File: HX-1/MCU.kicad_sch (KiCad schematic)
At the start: 27 parts, among them SW1 SW_SPDT, U1 STM32H723ZGT6

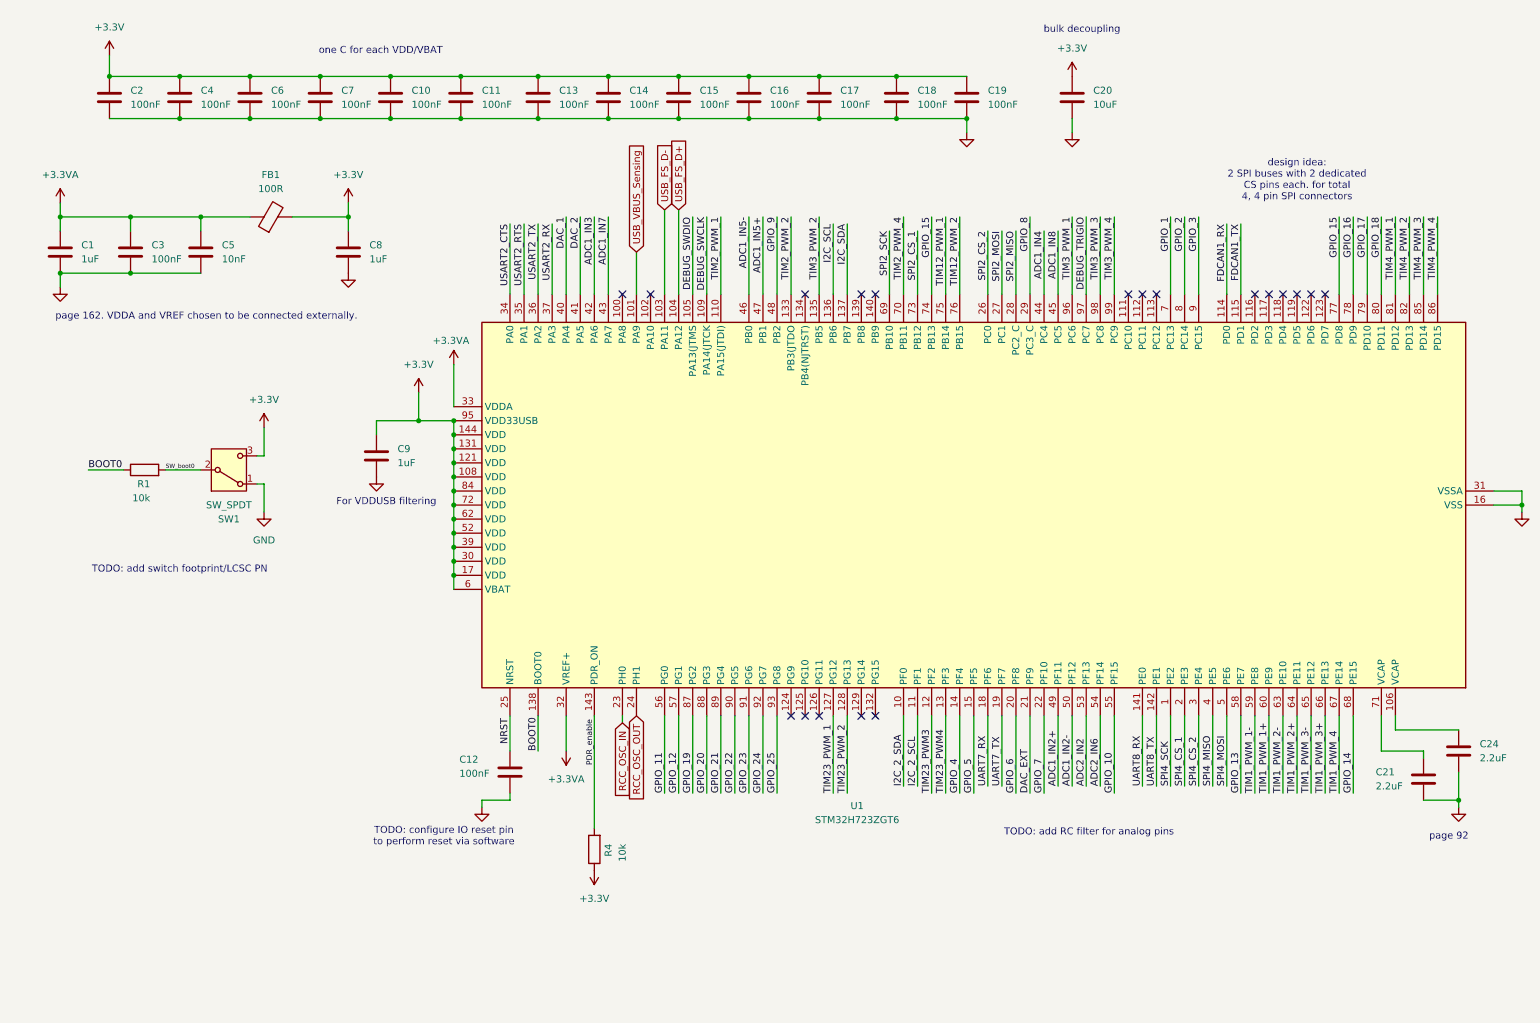
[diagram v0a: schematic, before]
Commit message: add buzzer, remove one ADC diff pair
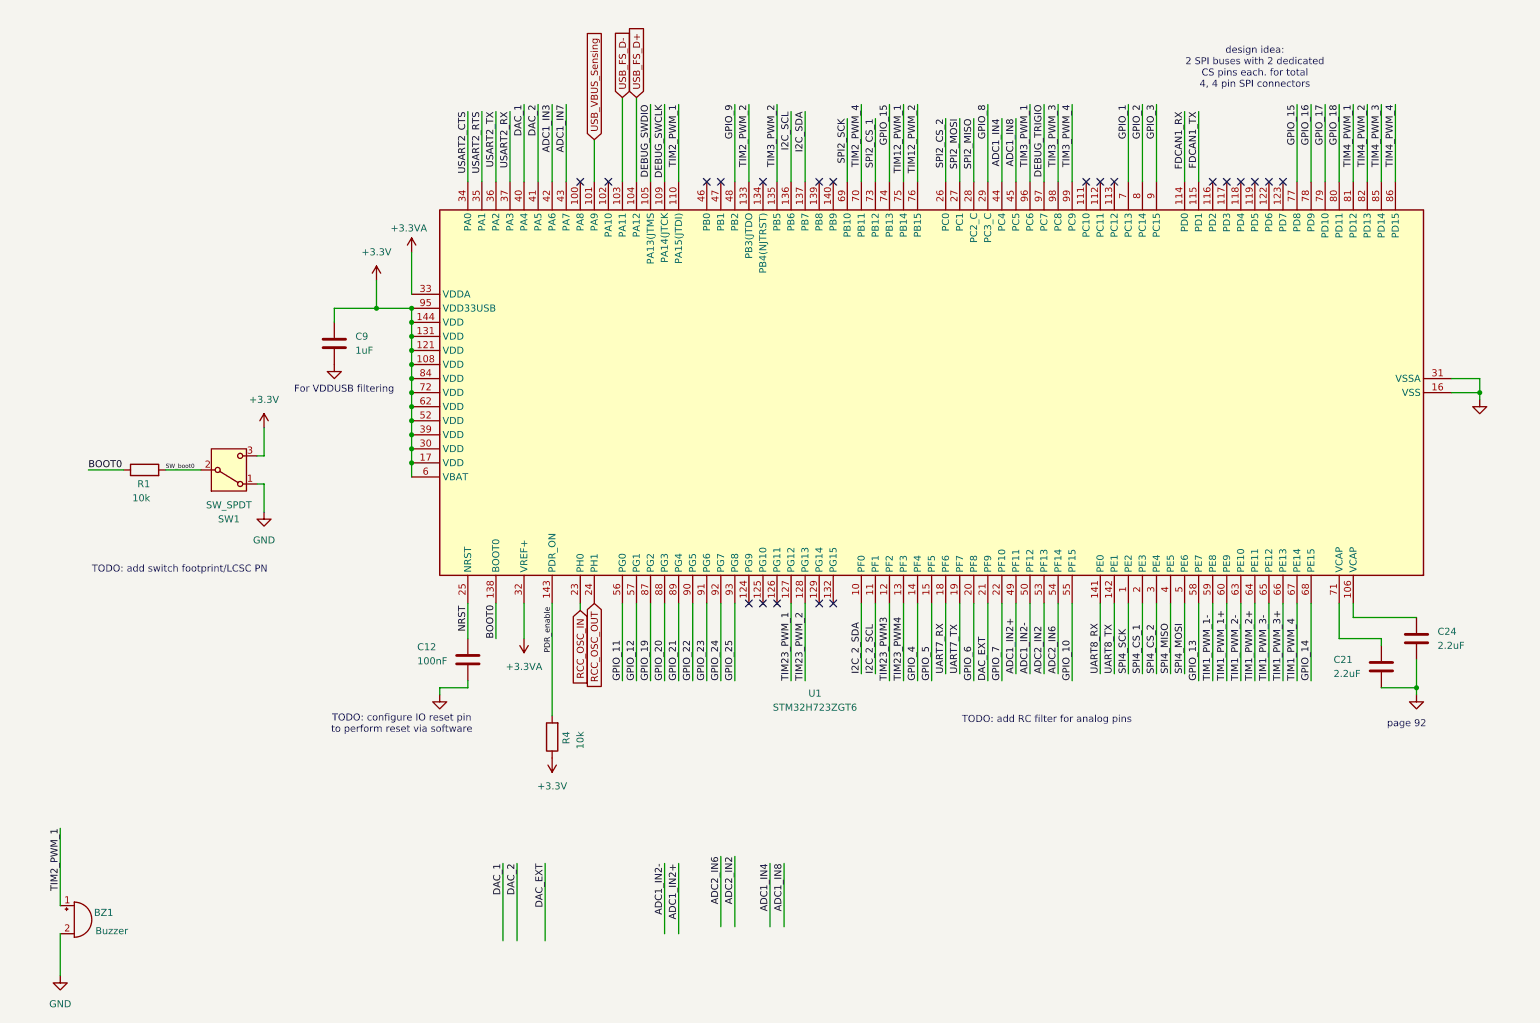
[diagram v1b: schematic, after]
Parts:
- removed C1, C8: 1uF, Capacitor_SMD:C_0603_1608Metric, symbol Device:C
- removed C10, C11, C13, C14, C15, C16, C17, C18, C19, C2, C3, C4, C6, C7: 100nF, Capacitor_SMD:C_0603_1608Metric, symbol Device:C
- removed C20: 10uF, Capacitor_SMD:C_0603_1608Metric, symbol Device:C
- removed C5: 10nF, Capacitor_SMD:C_0603_1608Metric, symbol Device:C
- removed FB1: 100R, Resistor_SMD:R_0805_2012Metric, symbol Device:FerriteBead
- added BZ1: Buzzer, Buzzer:YUEXIN YX-SMD5020, symbol Device:Buzzer
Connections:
- net GND: now also BZ1.2 (+)
- net TIM2_PWM_1: now also BZ1.1 (-)
- net ADC1_IN5+: no longer names the net of U1.47 (PB1)
- net ADC1_IN5-: no longer names the net of U1.46 (PB0)
- no-connect marks 19 -> 21
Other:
- note removed: "bulk decoupling"
- note removed: "one C for each VDD/VBAT"
- note removed: "page 162. VDDA and VREF chosen to be connected externally."
- moved on the sheet: C12, C21, C24, C9, R4, U1

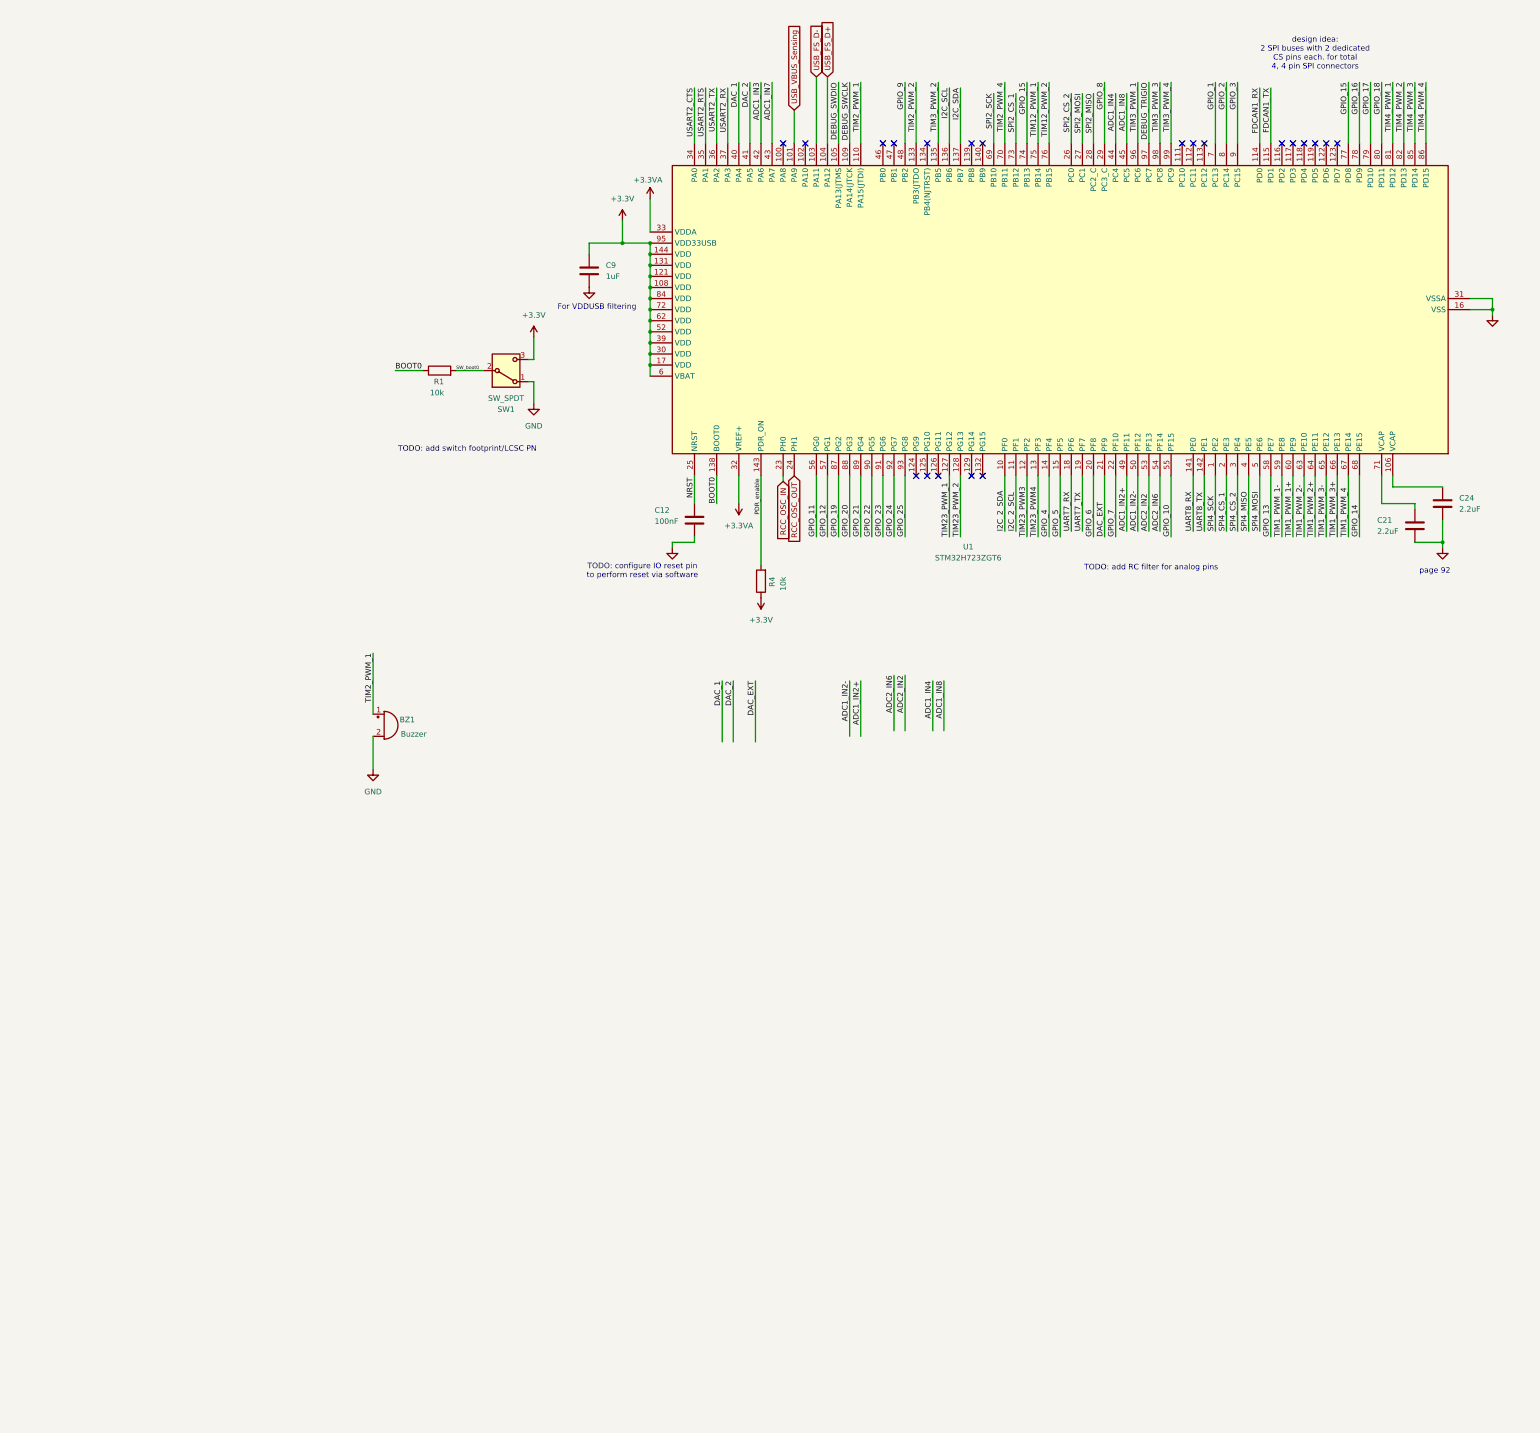
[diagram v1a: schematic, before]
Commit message: remove uart7, spi2 and extra CS. Not needed. Start mapping GPIO
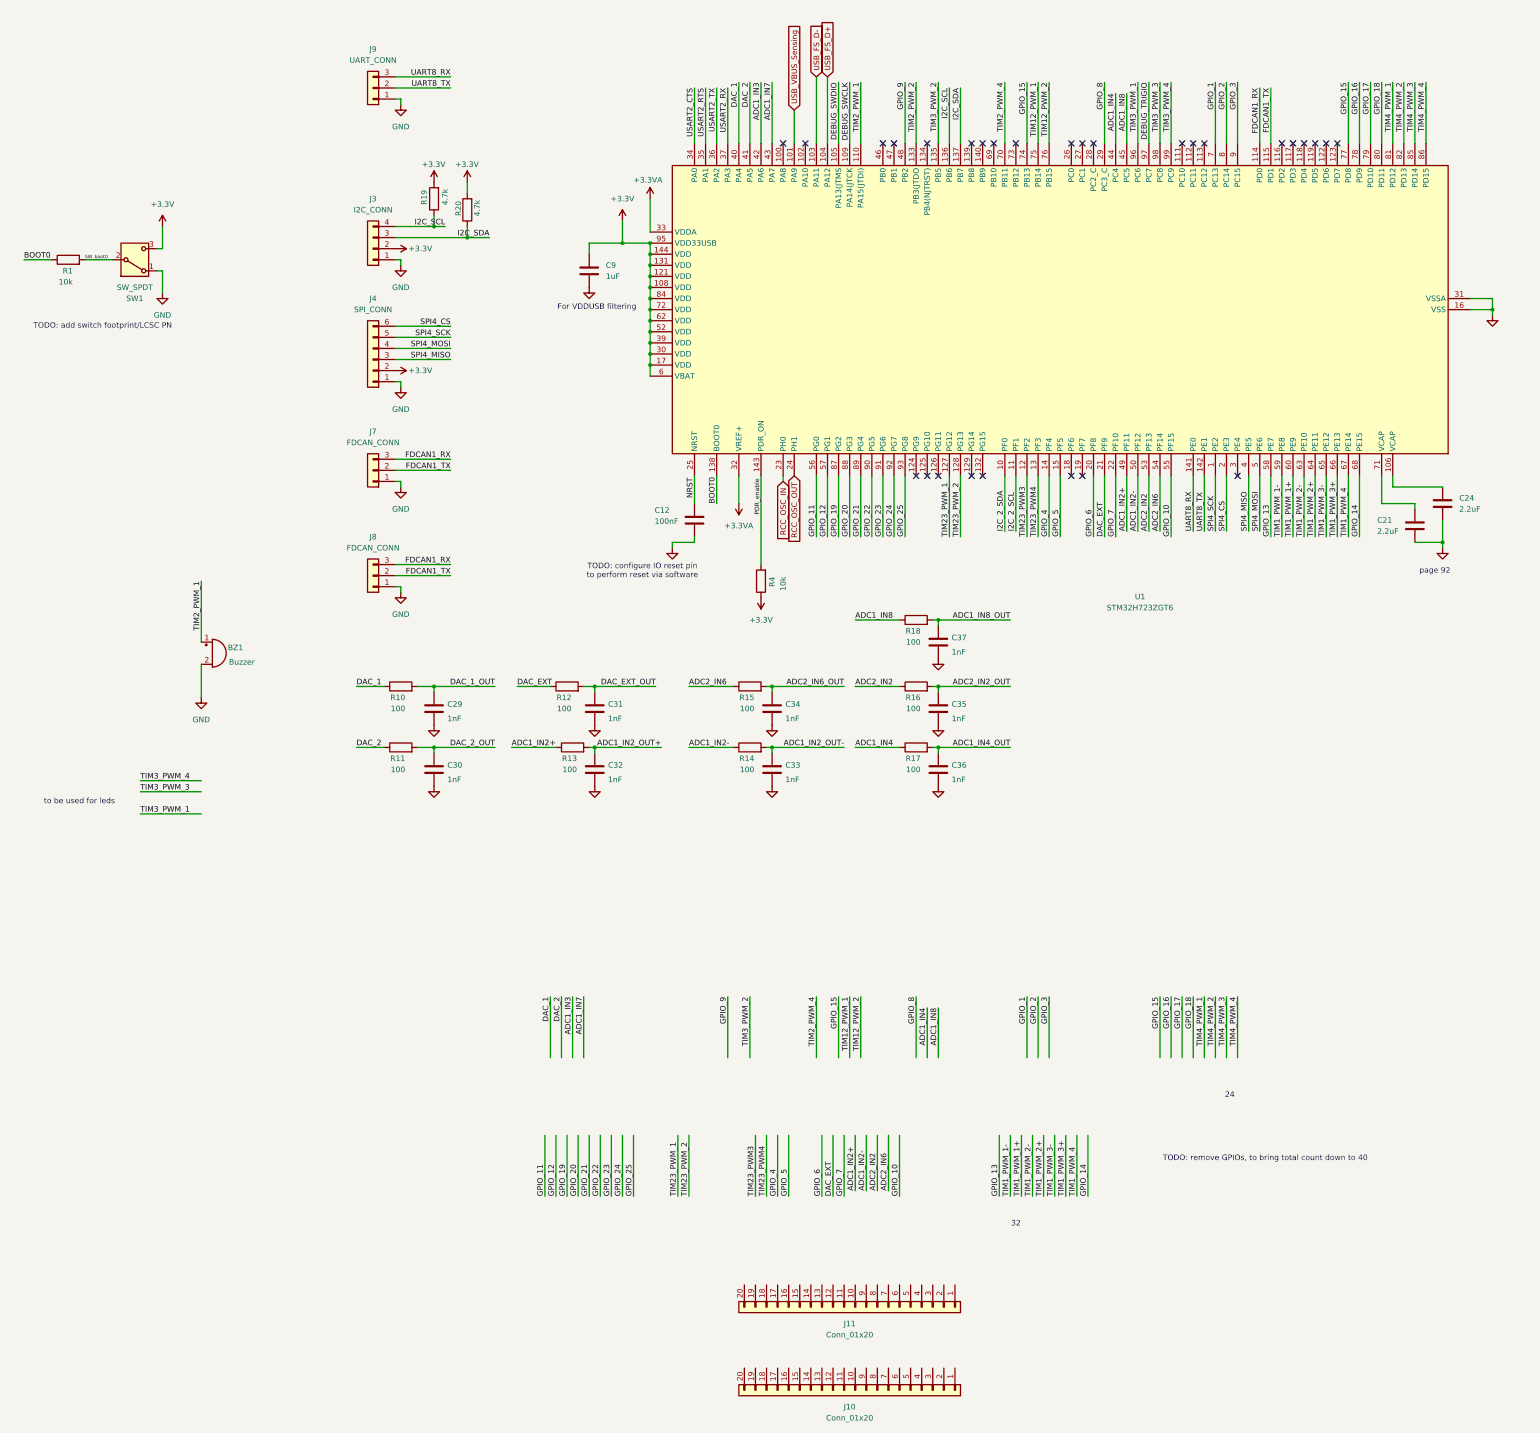
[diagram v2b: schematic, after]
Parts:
- added C29, C30, C31, C32, C33, C34, C35, C36, C37: 1nF, Capacitor_SMD:C_0603_1608Metric, symbol Device:C
- added J10, J11: Conn_01x20, Connector_PinHeader_2.54mm:PinHeader_1x20_P2.54mm_Vertical, symbol Connector_Generic:Conn_01x20
- added J3: I2C_CONN, symbol Connector_Generic:Conn_01x04
- added J4: SPI_CONN, symbol Connector_Generic:Conn_01x06
- added J7, J8: FDCAN_CONN, symbol Connector_Generic:Conn_01x03
- added J9: UART_CONN, symbol Connector_Generic:Conn_01x03
- added R10, R11, R12, R13, R14, R15, R16, R17, R18: 100, Resistor_SMD:R_0603_1608Metric, symbol Device:R
- added R19, R20: 4.7k, Resistor_SMD:R_0603_1608Metric, symbol Device:R
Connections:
- net +3.3V: now also J3.2 (Pin_2), J4.2 (Pin_2), R19.2, R20.2
- net ADC1_IN2+: now also R13.1
- net ADC1_IN2-: now also R14.1
- net ADC1_IN4: now also R17.1
- net ADC1_IN8: now also R18.1
- net ADC2_IN2: now also R16.1
- net ADC2_IN6: now also R15.1
- net DAC_1: now also R10.1
- net DAC_2: now also R11.1
- net DAC_EXT: now also R12.1
- net FDCAN1_RX: now also J7.3 (Pin_3), J8.3 (Pin_3)
- net FDCAN1_TX: now also J7.2 (Pin_2), J8.2 (Pin_2)
- net GND: now also C29.2, C30.2, C31.2, C32.2, C33.2, C34.2, C35.2, C36.2, C37.2, J3.1 (Pin_1), J4.1 (Pin_1), J7.1 (Pin_1), J8.1 (Pin_1), J9.1 (Pin_1)
- net I2C_SCL: now also J3.4 (Pin_4), R19.1
- net I2C_SDA: now also J3.3 (Pin_3), R20.1
- net SPI4_MISO: now also J4.3 (Pin_3)
- net SPI4_MOSI: now also J4.4 (Pin_4)
- net SPI4_SCK: now also J4.5 (Pin_5)
- net UART8_RX: now also J9.3 (Pin_3)
- net UART8_TX: now also J9.2 (Pin_2)
- net SPI2_CS_1: no longer names the net of U1.73 (PB12)
- net SPI2_CS_2: no longer names the net of U1.26 (PC0)
- net SPI2_MISO: no longer names the net of U1.28 (PC2_C)
- net SPI2_MOSI: no longer names the net of U1.27 (PC1)
- net SPI2_SCK: no longer names the net of U1.69 (PB10)
- net SPI4_CS_1 renamed SPI4_CS
- net SPI4_CS: now also J4.6 (Pin_6)
- net SPI4_CS_2: no longer names the net of U1.3 (PE4)
- net UART7_RX: no longer names the net of U1.18 (PF6)
- net UART7_TX: no longer names the net of U1.19 (PF7)
- new net ADC1_IN2_OUT+: C32.1, R13.2
- new net ADC1_IN2_OUT-: C33.1, R14.2
- new net ADC1_IN4_OUT: C36.1, R17.2
- new net ADC1_IN8_OUT: C37.1, R18.2
- new net ADC2_IN2_OUT: C35.1, R16.2
- new net ADC2_IN6_OUT: C34.1, R15.2
- new net DAC_1_OUT: C29.1, R10.2
- new net DAC_2_OUT: C30.1, R11.2
- new net DAC_EXT_OUT: C31.1, R12.2
- no-connect marks 21 -> 29
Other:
- note added: "24"
- note added: "32"
- note added: "TODO: remove GPIOs, to bring total count down to 40"
- note added: "to be used for leds"
- note removed: "TODO: add RC filter for analog pins"
- note removed: "design idea: 2 SPI buses with 2 dedicated CS pins each. for total 4, 4 pin SPI connectors"
- moved on the sheet: BZ1, R1, SW1
